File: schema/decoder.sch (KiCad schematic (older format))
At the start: 17 parts, among them Q1 BC177, U1 7402, U2 HEF4526B, U3 TLC555

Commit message: reannotate schema
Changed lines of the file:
@@
 $Descr A4 11693 8268
 encoding utf-8
-Sheet 6 6
+Sheet 5 6
 Title ""
 Date ""
@@
 $EndComp
 $Comp
-L GND #PWR30
+L GND #PWR27
 U 1 1 58C0583B
 P 3350 4500
-F 0 "#PWR30" H 3350 4250 50  0001 C CNN
+F 0 "#PWR27" H 3350 4250 50  0001 C CNN
 F 1 "GND" H 3350 4350 50  0000 C CNN
 F 2 "" H 3350 4500 50  0000 C CNN
@@
 $EndComp
 $Comp
-L +5V #PWR33
+L +5V #PWR30
 U 1 1 58C05885
 P 4250 800
-F 0 "#PWR33" H 4250 650 50  0001 C CNN
+F 0 "#PWR30" H 4250 650 50  0001 C CNN
 F 1 "+5V" H 4250 940 50  0000 C CNN
 F 2 "" H 4250 800 50  0000 C CNN
@@
 $EndComp
 $Comp
-L GND #PWR37
+L GND #PWR34
 U 1 1 58C05E32
 P 6850 6350
-F 0 "#PWR37" H 6850 6100 50  0001 C CNN
+F 0 "#PWR34" H 6850 6100 50  0001 C CNN
 F 1 "GND" H 6850 6200 50  0000 C CNN
 F 2 "" H 6850 6350 50  0000 C CNN
@@
 $EndComp
 $Comp
-L GND #PWR41
+L GND #PWR38
 U 1 1 58C061DE
 P 7650 3300
-F 0 "#PWR41" H 7650 3050 50  0001 C CNN
+F 0 "#PWR38" H 7650 3050 50  0001 C CNN
 F 1 "GND" H 7650 3150 50  0000 C CNN
 F 2 "" H 7650 3300 50  0000 C CNN
@@
 $EndComp
 $Comp
-L GND #PWR39
+L GND #PWR36
 U 1 1 58C0698F
 P 7100 4200
-F 0 "#PWR39" H 7100 3950 50  0001 C CNN
+F 0 "#PWR36" H 7100 3950 50  0001 C CNN
 F 1 "GND" H 7100 4050 50  0000 C CNN
 F 2 "" H 7100 4200 50  0000 C CNN
@@
 $EndComp
 $Comp
-L GND #PWR42
+L GND #PWR39
 U 1 1 58C06B39
 P 8250 3350
-F 0 "#PWR42" H 8250 3100 50  0001 C CNN
+F 0 "#PWR39" H 8250 3100 50  0001 C CNN
 F 1 "GND" H 8250 3200 50  0000 C CNN
 F 2 "" H 8250 3350 50  0000 C CNN
@@
 $EndComp
 $Comp
-L GND #PWR35
+L GND #PWR32
 U 1 1 58C07F5B
 P 5400 6000
-F 0 "#PWR35" H 5400 5750 50  0001 C CNN
+F 0 "#PWR32" H 5400 5750 50  0001 C CNN
 F 1 "GND" H 5400 5850 50  0000 C CNN
 F 2 "" H 5400 6000 50  0000 C CNN
@@
 $EndComp
 $Comp
-L GND #PWR31
+L GND #PWR28
 U 1 1 58C08807
 P 3500 6250
-F 0 "#PWR31" H 3500 6000 50  0001 C CNN
+F 0 "#PWR28" H 3500 6000 50  0001 C CNN
 F 1 "GND" H 3500 6100 50  0000 C CNN
 F 2 "" H 3500 6250 50  0000 C CNN
@@
 $EndComp
 $Comp
-L GND #PWR36
+L GND #PWR33
 U 1 1 58C08D75
 P 5550 5650
-F 0 "#PWR36" H 5550 5400 50  0001 C CNN
+F 0 "#PWR33" H 5550 5400 50  0001 C CNN
 F 1 "GND" H 5550 5500 50  0000 C CNN
 F 2 "" H 5550 5650 50  0000 C CNN
@@
 $EndComp
 $Comp
-L +5V #PWR29
+L +5V #PWR26
 U 1 1 58C8FF2B
 P 3150 3550
-F 0 "#PWR29" H 3150 3400 50  0001 C CNN
+F 0 "#PWR26" H 3150 3400 50  0001 C CNN
 F 1 "+5V" H 3150 3690 50  0000 C CNN
 F 2 "" H 3150 3550 50  0000 C CNN
@@
 $EndComp
 $Comp
-L +5V #PWR32
+L +5V #PWR29
 U 1 1 58C9031F
 P 3750 3100
-F 0 "#PWR32" H 3750 2950 50  0001 C CNN
+F 0 "#PWR29" H 3750 2950 50  0001 C CNN
 F 1 "+5V" H 3750 3240 50  0000 C CNN
 F 2 "" H 3750 3100 50  0000 C CNN
@@
 $EndComp
 $Comp
-L GND #PWR34
+L GND #PWR31
 U 1 1 58C90F7F
 P 5100 2050
-F 0 "#PWR34" H 5100 1800 50  0001 C CNN
+F 0 "#PWR31" H 5100 1800 50  0001 C CNN
 F 1 "GND" H 5100 1900 50  0000 C CNN
 F 2 "" H 5100 2050 50  0000 C CNN
@@
 NoConn ~ 4650 3950
 $Comp
-L +5V #PWR38
+L +5V #PWR35
 U 1 1 58C91824
 P 7100 2050
-F 0 "#PWR38" H 7100 1900 50  0001 C CNN
+F 0 "#PWR35" H 7100 1900 50  0001 C CNN
 F 1 "+5V" H 7100 2190 50  0000 C CNN
 F 2 "" H 7100 2050 50  0000 C CNN
@@
 $EndComp
 $Comp
-L +5V #PWR40
+L +5V #PWR37
 U 1 1 58C91A38
 P 7650 2400
-F 0 "#PWR40" H 7650 2250 50  0001 C CNN
+F 0 "#PWR37" H 7650 2250 50  0001 C CNN
 F 1 "+5V" H 7650 2540 50  0000 C CNN
 F 2 "" H 7650 2400 50  0000 C CNN
@@
 $EndComp
 $Comp
-L +5V #PWR43
+L +5V #PWR40
 U 1 1 58C91BDC
 P 8600 2350
-F 0 "#PWR43" H 8600 2200 50  0001 C CNN
+F 0 "#PWR40" H 8600 2200 50  0001 C CNN
 F 1 "+5V" H 8600 2490 50  0000 C CNN
 F 2 "" H 8600 2350 50  0000 C CNN
@@
 Connection ~ 4950 1800
 Wire Wire Line
-	4950 1650 4950 1800
-Wire Wire Line
-	4950 1800 4950 1950
-Wire Wire Line
-	4950 1950 4950 2100
+	4950 1650 4950 2100
 Connection ~ 4400 2100
 Wire Wire Line
@@
 	4650 1950 4300 1950
 Wire Wire Line
-	4400 1550 4400 2100
-Wire Wire Line
-	4400 2100 4400 3200
-Wire Wire Line
-	4300 1550 4300 1950
-Wire Wire Line
-	4300 1950 4300 3200
+	4400 1550 4400 3200
+Wire Wire Line
+	4300 1550 4300 3200
 Connection ~ 4200 1800
 Wire Wire Line
@@
 	4650 1650 4100 1650
 Wire Wire Line
-	4100 950  4200 950
-Wire Wire Line
-	4200 950  4250 950
-Wire Wire Line
-	4250 950  4300 950
-Wire Wire Line
-	4300 950  4400 950
+	4100 950  4400 950
 Connection ~ 4250 950
 Wire Wire Line
@@
 	5550 5650 5550 5650
 Wire Wire Line
-	3400 5350 5300 5350
-Wire Wire Line
-	5300 5350 5550 5350
-Wire Wire Line
-	5550 5350 5700 5350
+	3400 5350 5700 5350
 Wire Wire Line
 	3400 5350 3400 5600
@@
 	3500 5800 3500 5950
 Wire Wire Line
-	3400 5800 3500 5800
-Wire Wire Line
-	3500 5800 3650 5800
+	3400 5800 3650 5800
 Wire Wire Line
 	3950 5800 4100 5800
@@
 Connection ~ 8600 2900
 Wire Wire Line
-	8600 2700 8600 2900
-Wire Wire Line
-	8600 2900 8600 5350
-Wire Wire Line
-	8600 5350 8600 5950
+	8600 2700 8600 5950
 Wire Wire Line
 	8150 2900 8600 2900
@@
 Connection ~ 7100 4100
 Wire Wire Line
-	7100 4050 7100 4100
-Wire Wire Line
-	7100 4100 7100 4200
+	7100 4050 7100 4200
 Wire Wire Line
 	7300 4100 7100 4100
@@
 	7100 3000 7150 3000
 Wire Wire Line
-	7100 2500 7100 2700
-Wire Wire Line
-	7100 2700 7100 3000
-Wire Wire Line
-	7100 3000 7100 3600
-Wire Wire Line
-	7100 3600 7100 3650
+	7100 2500 7100 3650
 Wire Wire Line
 	3350 3750 3350 2900
@@
 	6700 3850 6800 3850
 Wire Wire Line
-	1650 2900 3350 2900
-Wire Wire Line
-	3350 2900 6700 2900
-Wire Wire Line
-	6700 2900 7150 2900
+	1650 2900 7150 2900
 Wire Wire Line
 	6700 2900 6700 3850
@@
 	3950 4350 3350 4350
 Wire Wire Line
-	3350 4000 3350 4350
-Wire Wire Line
-	3350 4350 3350 4500
+	3350 4000 3350 4500
 Wire Wire Line
 	3450 4000 3350 4000
@@
 	3150 4100 3450 4100
 Wire Wire Line
-	3150 3550 3150 3650
-Wire Wire Line
-	3150 3650 3150 4100
+	3150 3550 3150 4100
 Wire Wire Line
 	3450 3650 3150 3650
@@
 Connection ~ 4200 950
 Wire Wire Line
-	4200 1550 4200 1800
-Wire Wire Line
-	4200 1800 4200 3200
-Wire Wire Line
-	4100 1550 4100 1650
-Wire Wire Line
-	4100 1650 4100 3200
+	4200 1550 4200 3200
+Wire Wire Line
+	4100 1550 4100 3200
 Wire Wire Line
 	2050 5700 2050 2700

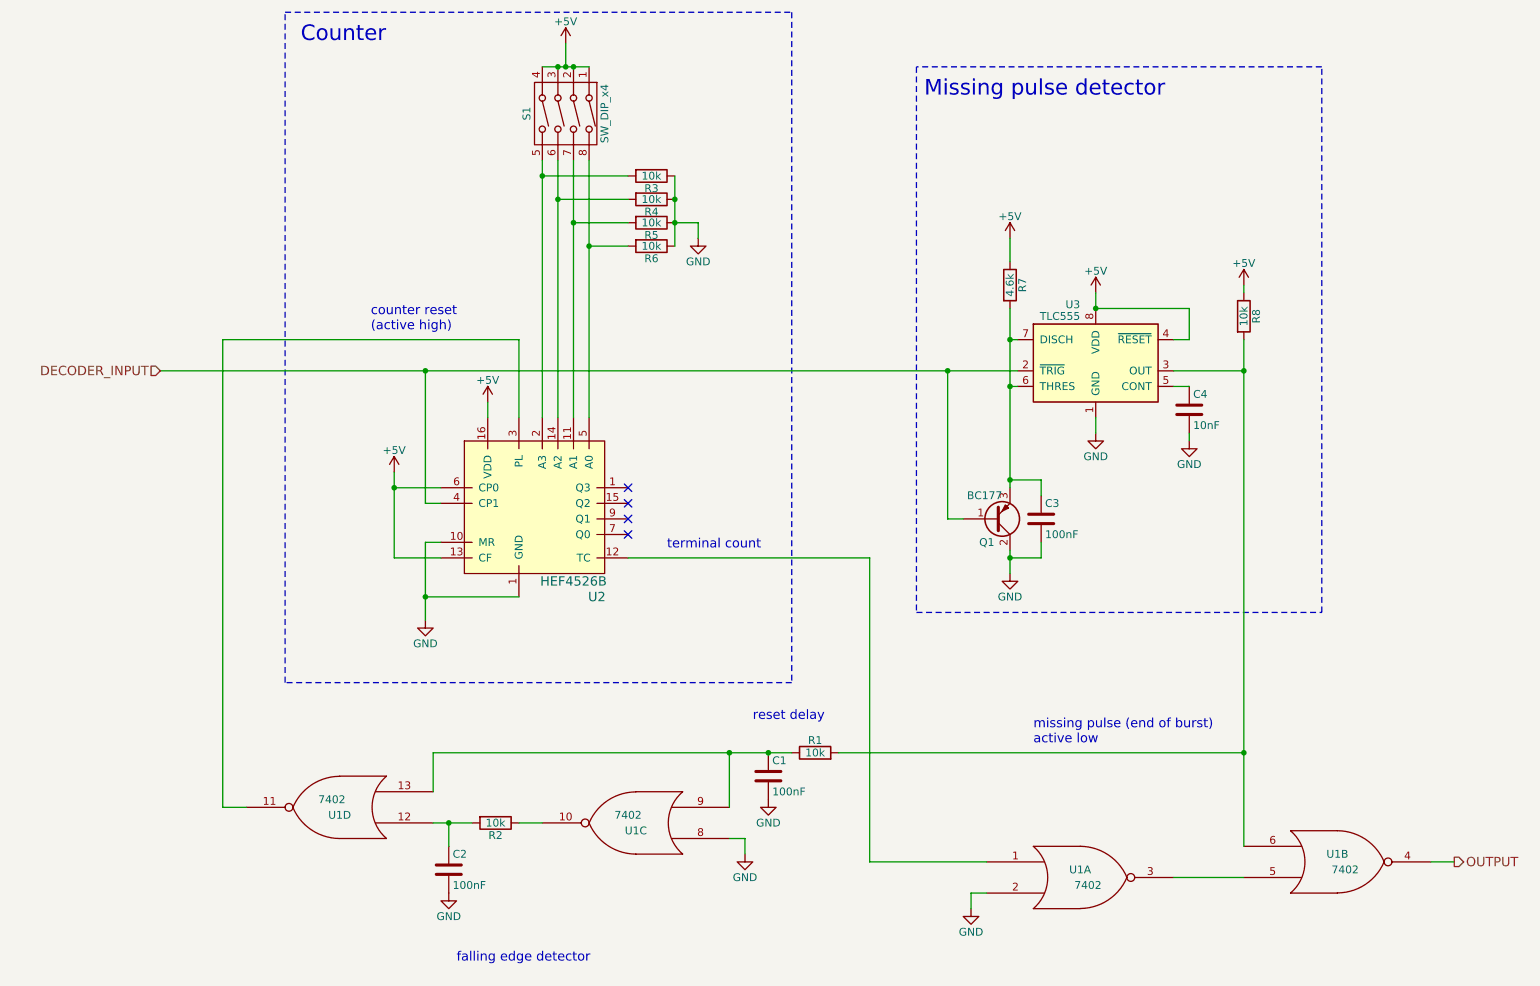
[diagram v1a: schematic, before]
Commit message: Schematic done
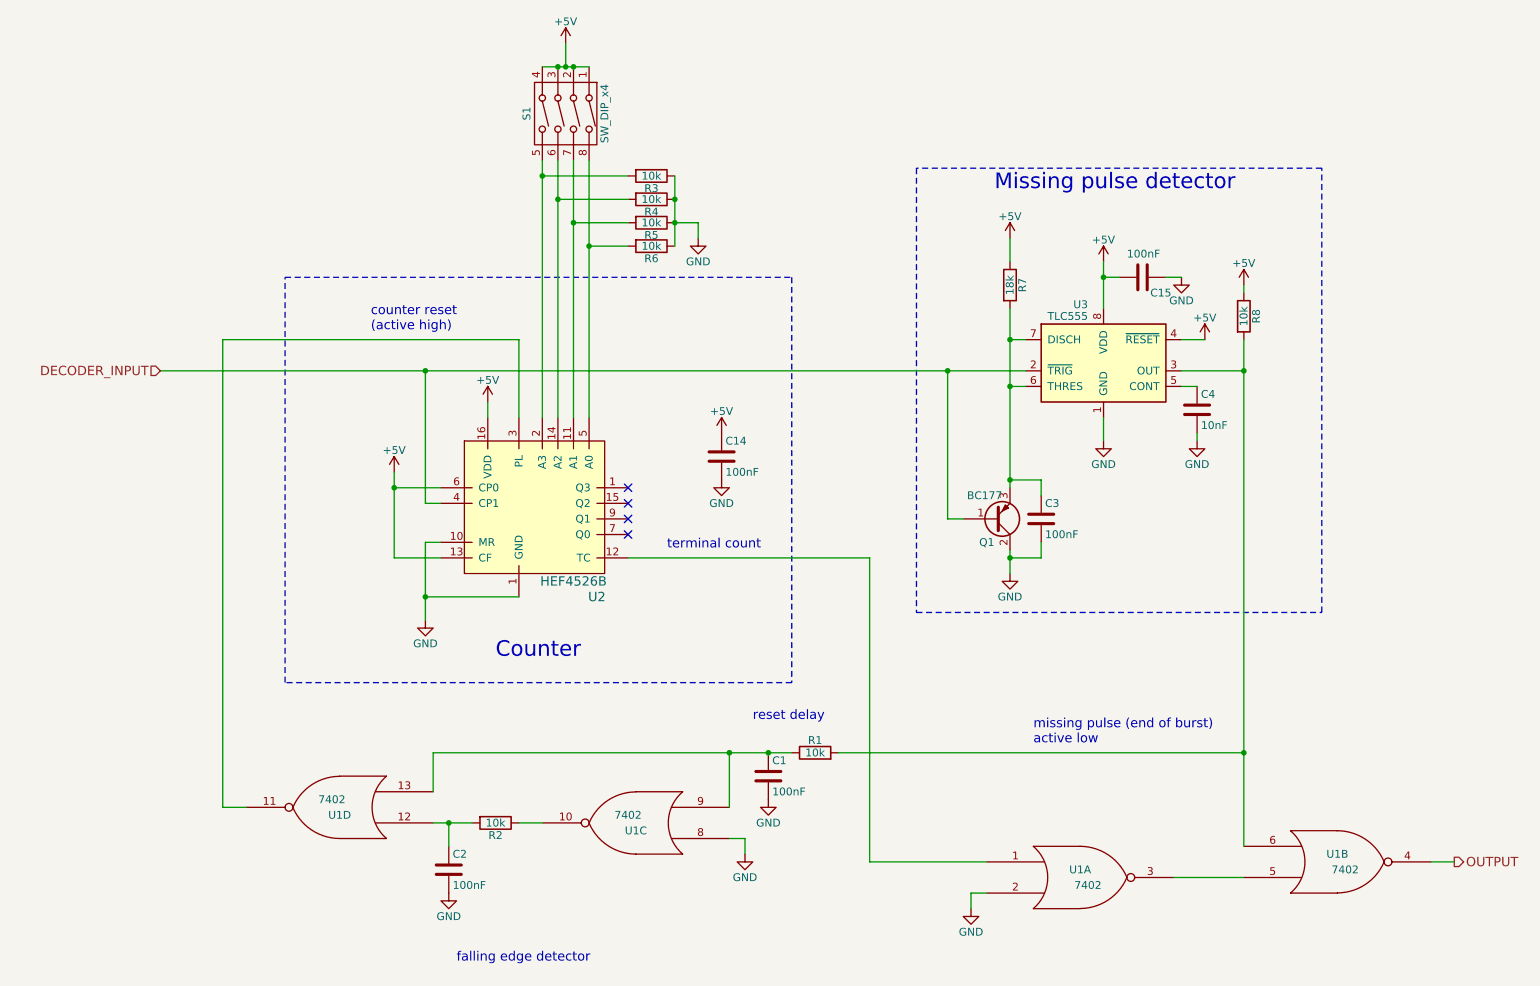
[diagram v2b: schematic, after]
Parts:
- added C14, C15: 100nF, symbol C
- R7: value 4.6k -> 18k
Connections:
- net +5V: now also C14.1, C15.2
- net GND: now also C14.2, C15.1
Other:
- moved on the sheet: C4, U3
